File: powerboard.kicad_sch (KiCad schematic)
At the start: 6 parts, among them J3 Conn_02x04, J4 Conn_02x04, J5 Conn_02x04

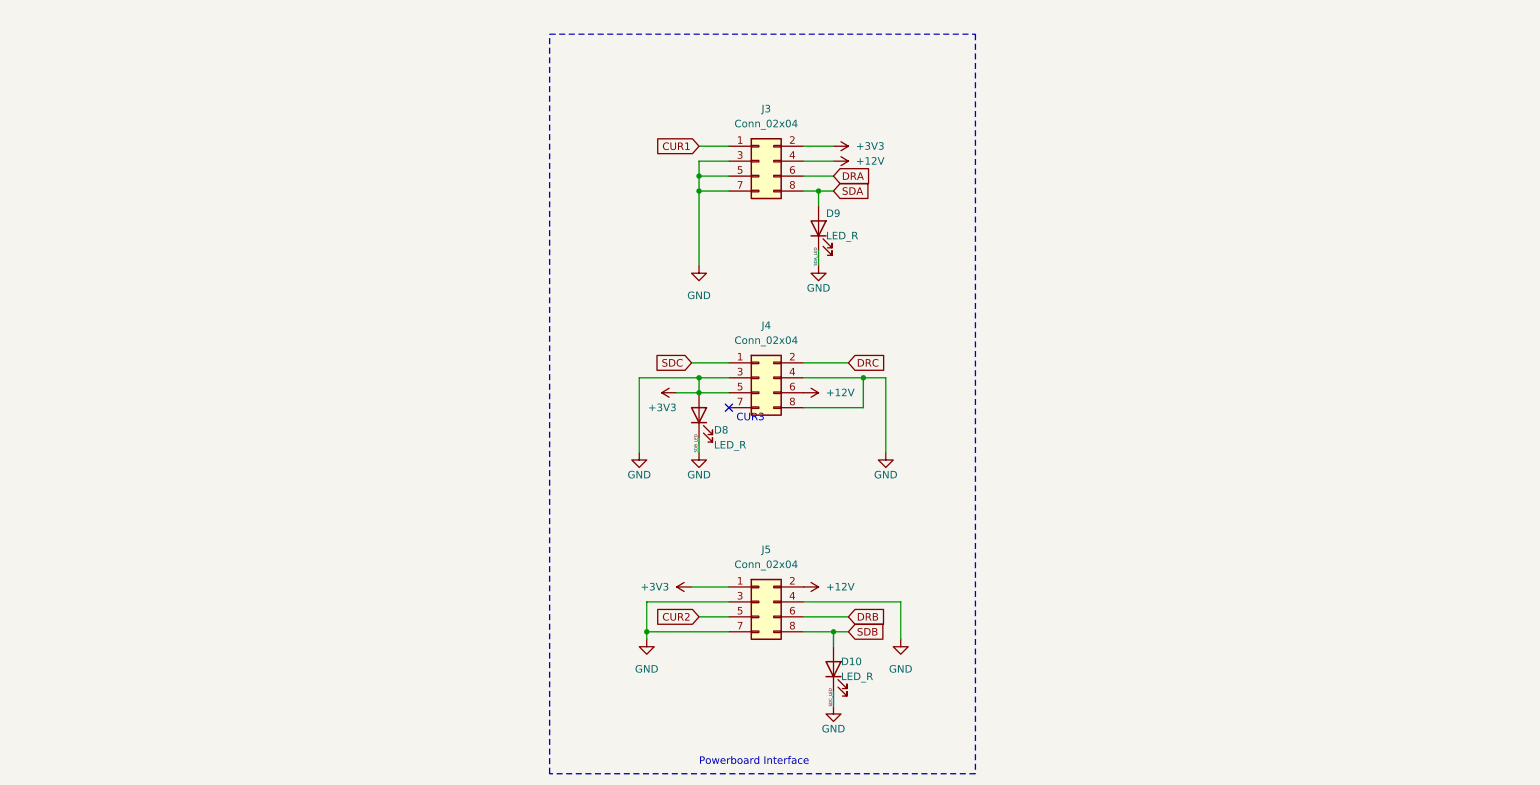
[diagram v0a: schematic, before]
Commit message: Fixed short cirquit, minors
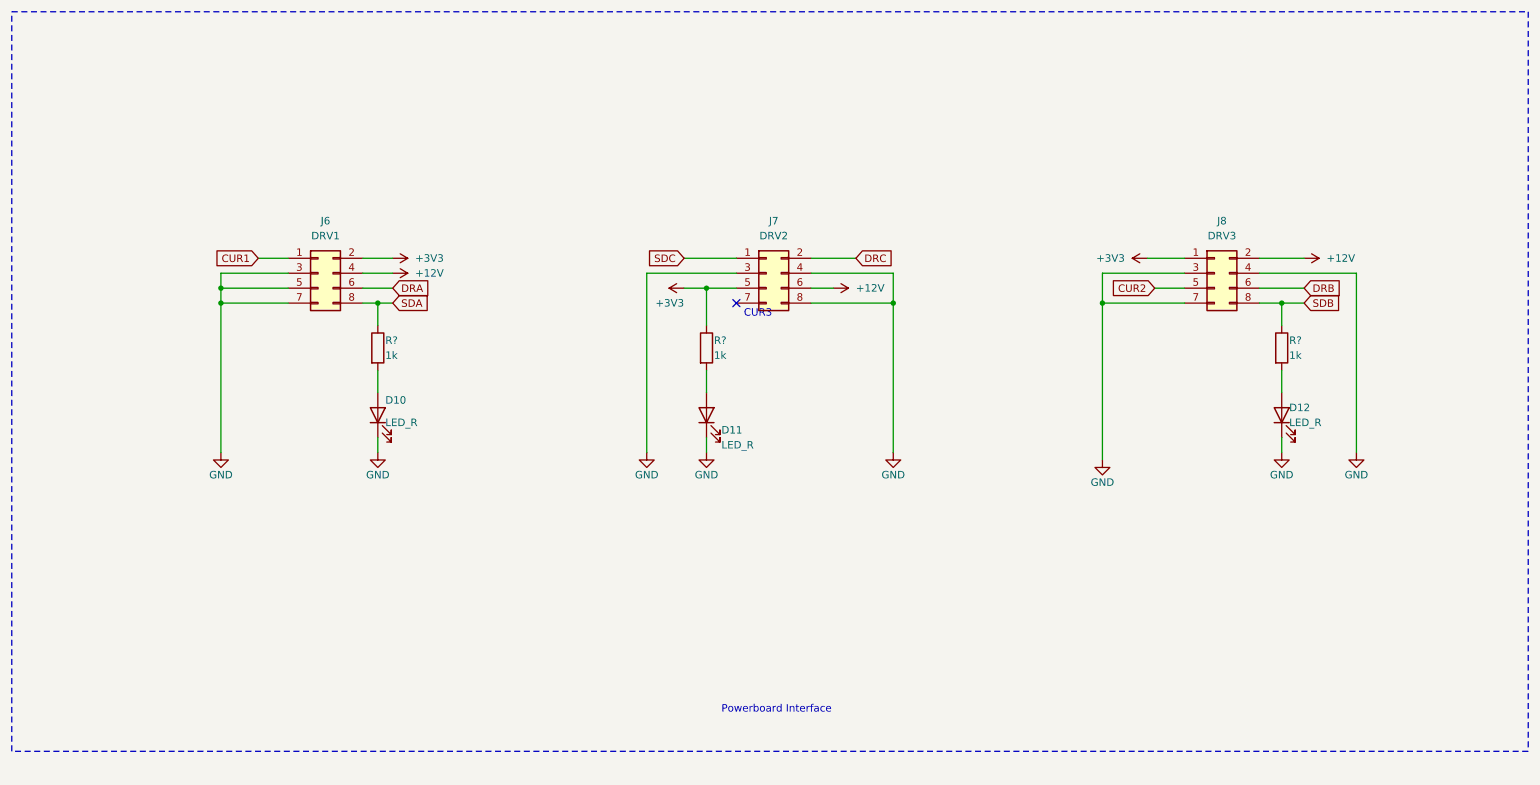
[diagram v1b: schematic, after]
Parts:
- removed D8, D9: LED_R, LED_SMD:LED_0603_1608Metric, symbol Device:LED
- removed J3, J4, J5: Conn_02x04, Connector_PinSocket_2.54mm:PinSocket_2x04_P2.54mm_Vertical, symbol PCM_4ms_Connector:Conn_02x04
- added D11, D12: LED_R, LED_SMD:LED_0603_1608Metric, symbol Device:LED
- added J6: DRV1, symbol Connector_Generic:Conn_02x04_Odd_Even
- added J7: DRV2, symbol Connector_Generic:Conn_02x04_Odd_Even
- added J8: DRV3, symbol Connector_Generic:Conn_02x04_Odd_Even
- added R? (x3): 1k, Resistor_SMD:R_0603_1608Metric_Pad0.98x0.95mm_HandSolder, symbol Device:R
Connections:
- net +12V: now also J6.4 (Pin_4), J7.6 (Pin_6), J8.2 (Pin_2)
- net +3V3: now also J6.2 (Pin_2), J7.5 (Pin_5), J8.1 (Pin_1), R?.1; no longer D10.1 (K)
- net CUR1: now also J6.1 (Pin_1)
- net CUR2: now also J8.5 (Pin_5)
- net DRA: now also J6.6 (Pin_6)
- net DRB: now also J8.6 (Pin_6)
- net DRC: now also J7.2 (Pin_2)
- net SDA: now also J6.8 (Pin_8), R?.1
- net SDB: now also J8.8 (Pin_8), R?.1; no longer D10.2 (A)
- net SDC: now also J7.1 (Pin_1)
- new net: D10.2 (A), R?.2
- new net: D12.2 (A), R?.2
- new net: D11.2 (A), R?.2
- new net GND: D10.1 (K), D11.1 (K), D12.1 (K), J6.3 (Pin_3), J6.5 (Pin_5), J6.7 (Pin_7), J7.3 (Pin_3), J7.4 (Pin_4), J7.8 (Pin_8), J8.3 (Pin_3), J8.4 (Pin_4), J8.7 (Pin_7)

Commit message: Add drivers, stepdown on VIPER115, fixes
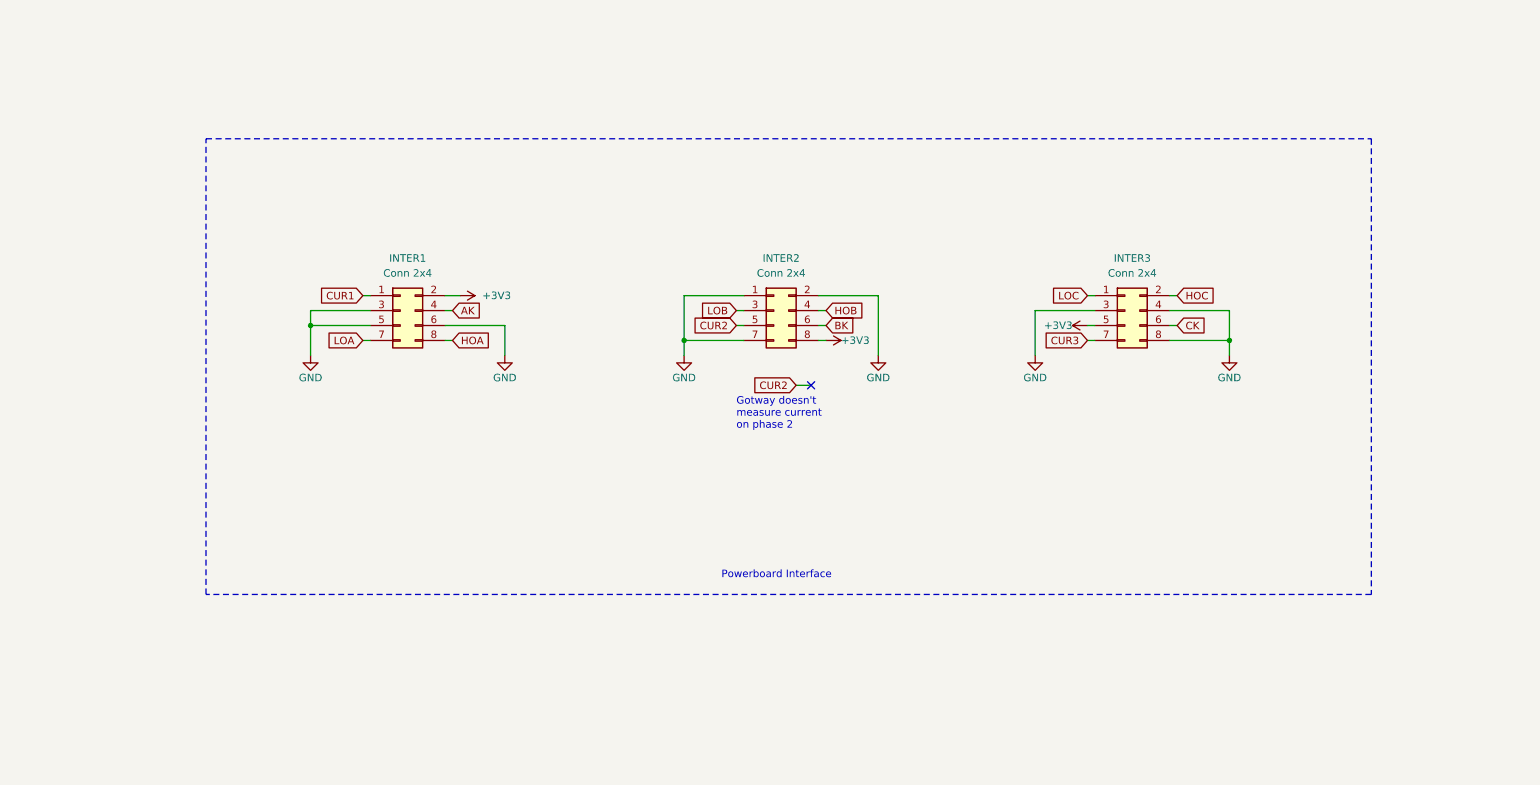
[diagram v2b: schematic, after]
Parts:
- removed D10, D11, D12: LED_R, LED_SMD:LED_0603_1608Metric, symbol Device:LED
- removed J6: DRV1, symbol Connector_Generic:Conn_02x04_Odd_Even
- removed J7: DRV2, symbol Connector_Generic:Conn_02x04_Odd_Even
- removed J8: DRV3, symbol Connector_Generic:Conn_02x04_Odd_Even
- removed R? (x3): 1k, Resistor_SMD:R_0603_1608Metric_Pad0.98x0.95mm_HandSolder, symbol Device:R
- added INTER1, INTER2, INTER3: Conn 2x4, Connector_PinHeader_2.54mm:PinHeader_2x04_P2.54mm_Vertical, symbol Connector_Generic:Conn_02x04_Odd_Even
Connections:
- net +3V3: now also INTER1.2 (Pin_2), INTER2.8 (Pin_8), INTER3.5 (Pin_5)
- net CUR1: now also INTER1.1 (Pin_1)
- net CUR2: now also INTER2.5 (Pin_5)
- net GND: now also INTER1.3 (Pin_3), INTER1.5 (Pin_5), INTER1.6 (Pin_6), INTER2.1 (Pin_1), INTER2.2 (Pin_2), INTER2.7 (Pin_7), INTER3.3 (Pin_3), INTER3.4 (Pin_4), INTER3.8 (Pin_8)
- new net AK: INTER1.4 (Pin_4)
- new net BK: INTER2.6 (Pin_6)
- new net CK: INTER3.6 (Pin_6)
- new net CUR3: INTER3.7 (Pin_7)
- new net HOA: INTER1.8 (Pin_8)
- new net HOB: INTER2.4 (Pin_4)
- new net HOC: INTER3.2 (Pin_2)
- new net LOA: INTER1.7 (Pin_7)
- new net LOB: INTER2.3 (Pin_3)
- new net LOC: INTER3.1 (Pin_1)
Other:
- note added: "Gotway doesn't measure current on phase 2"
- note removed: "CUR3"

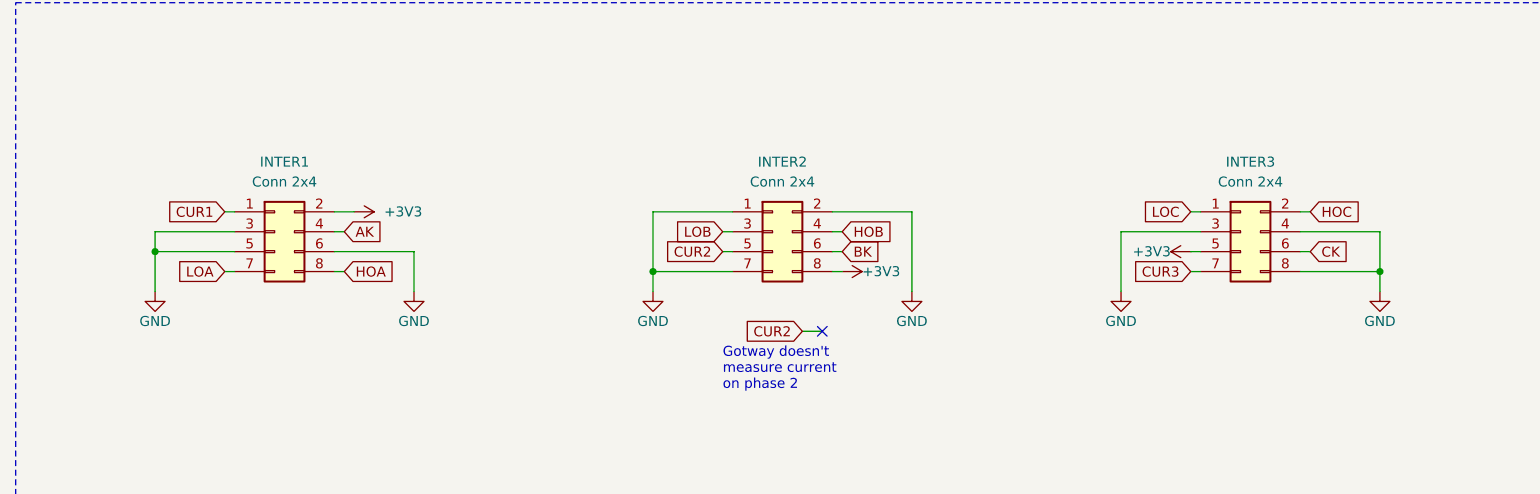
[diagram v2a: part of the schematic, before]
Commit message: Replaced unused GPIO, added SWD connectorm, PCB in progress
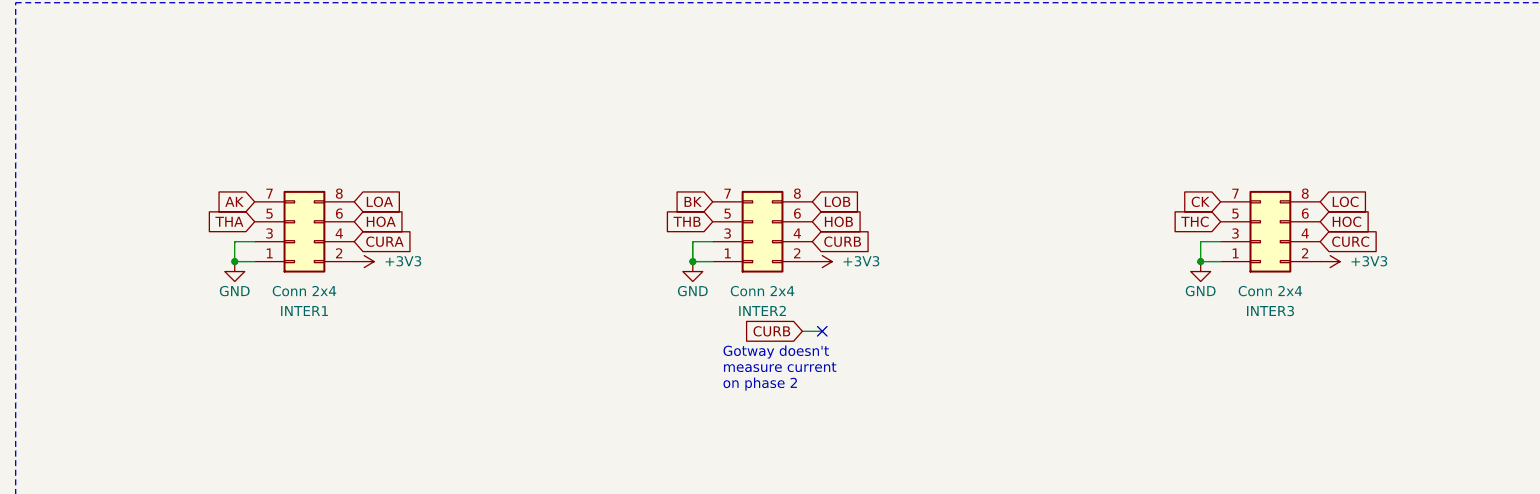
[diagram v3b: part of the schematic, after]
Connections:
- net CUR1 is gone; now on net GND: INTER1.1 (Pin_1)
- net CUR3 is gone; now on net CK: INTER3.7 (Pin_7)
- net +3V3: now also INTER2.2 (Pin_2), INTER3.2 (Pin_2); no longer INTER2.8 (Pin_8), INTER3.5 (Pin_5)
- net AK: now also INTER1.7 (Pin_7); no longer INTER1.4 (Pin_4)
- net BK: now also INTER2.7 (Pin_7); no longer INTER2.6 (Pin_6)
- net CK: no longer INTER3.6 (Pin_6)
- net GND: now also INTER2.3 (Pin_3), INTER3.1 (Pin_1); no longer INTER1.5 (Pin_5), INTER1.6 (Pin_6), INTER2.2 (Pin_2), INTER2.7 (Pin_7), INTER3.4 (Pin_4), INTER3.8 (Pin_8)
- net HOA: now also INTER1.6 (Pin_6); no longer INTER1.8 (Pin_8)
- net HOB: now also INTER2.6 (Pin_6); no longer INTER2.4 (Pin_4)
- net HOC: now also INTER3.6 (Pin_6); no longer INTER3.2 (Pin_2)
- net LOA: now also INTER1.8 (Pin_8); no longer INTER1.7 (Pin_7)
- net LOB: now also INTER2.8 (Pin_8); no longer INTER2.3 (Pin_3)
- net LOC: now also INTER3.8 (Pin_8); no longer INTER3.1 (Pin_1)
- net CUR2 renamed THB
- new net CURA: INTER1.4 (Pin_4)
- new net CURB: INTER2.4 (Pin_4)
- new net CURC: INTER3.4 (Pin_4)
- new net THA: INTER1.5 (Pin_5)
- new net THC: INTER3.5 (Pin_5)
